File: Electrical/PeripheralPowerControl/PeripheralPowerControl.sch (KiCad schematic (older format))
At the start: 6 parts, among them J1 Conn_01x03, J2 Screw_Terminal_01x02, J3 Conn_01x03

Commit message: Adds ground plane to the peripheral board
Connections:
- net GND: now reaches BUCK1.1 (IN-), J1.1 (Pin_1), J3.1 (Pin_1)
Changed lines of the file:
@@
 	2850 1150 2850 1900
 Connection ~ 2850 1900
+$Comp
+L power:GND #PWR?
+U 1 1 5D95AD47
+P 2850 3900
+F 0 "#PWR?" H 2850 3650 50  0001 C CNN
+F 1 "GND" H 2855 3727 50  0000 C CNN
+F 2 "" H 2850 3900 50  0001 C CNN
+F 3 "" H 2850 3900 50  0001 C CNN
+	1    2850 3900
+	1    0    0    -1
+$EndComp
+Connection ~ 2850 3900
 $EndSCHEMATC

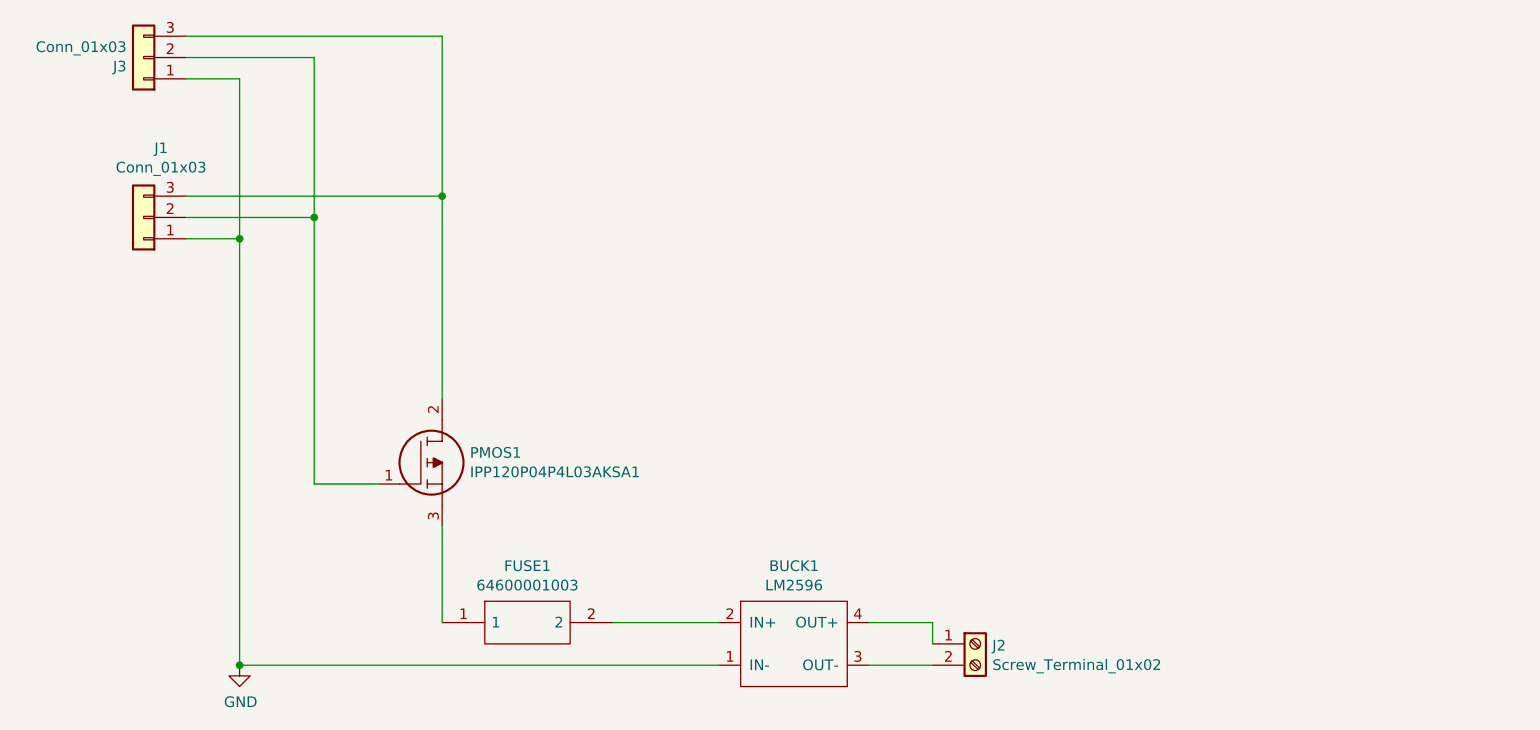
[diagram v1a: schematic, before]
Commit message: Verified Peripheral and Motor power controllers
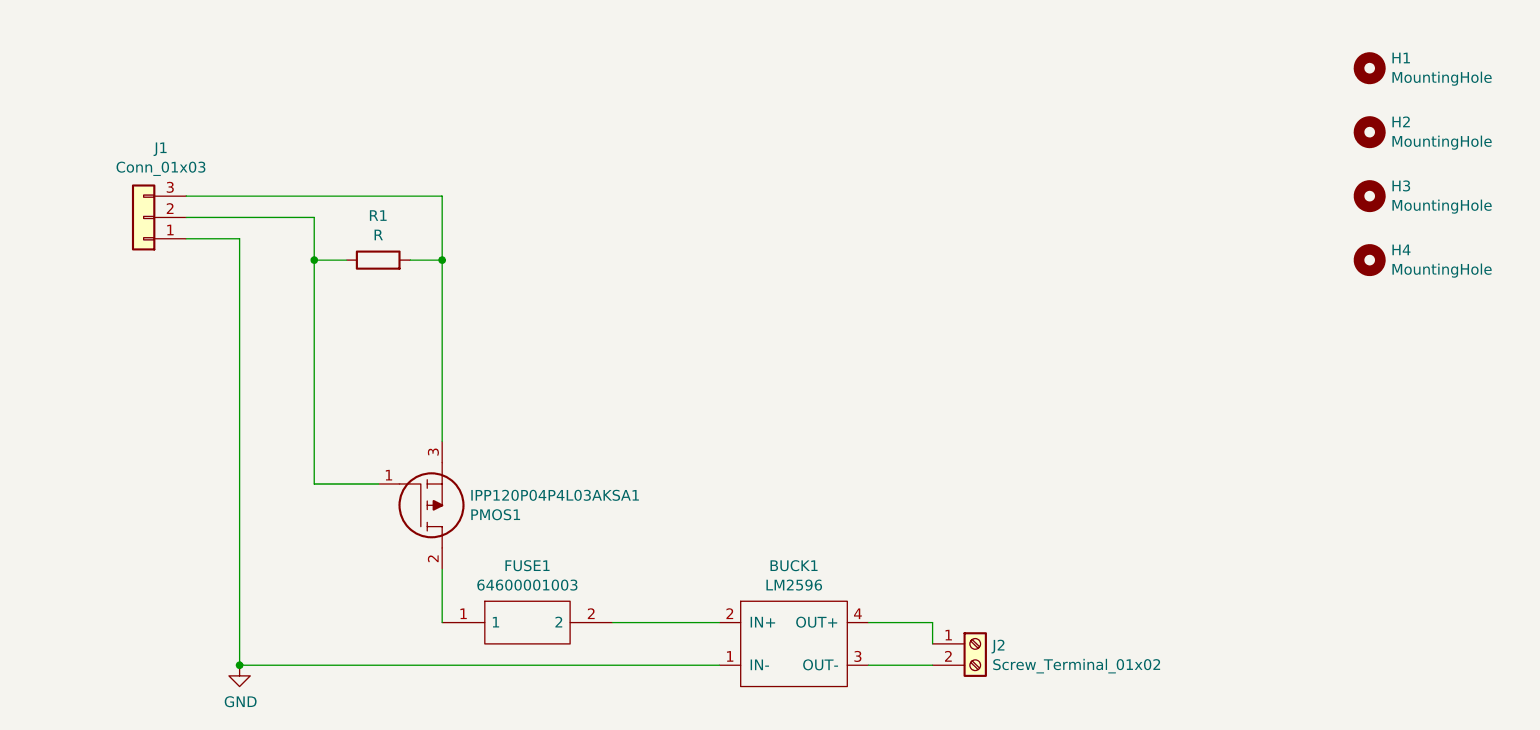
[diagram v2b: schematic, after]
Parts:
- removed J3: Conn_01x03, Connector_PinSocket_2.54mm:PinSocket_1x03_P2.54mm_Horizontal, symbol Connector_Generic:Conn_01x03
- added H1, H2, H3, H4: MountingHole, MountingHole:MountingHole_3.2mm_M3, symbol Mechanical:MountingHole
- added R1: R, Resistor_THT:R_Axial_DIN0204_L3.6mm_D1.6mm_P7.62mm_Horizontal, symbol Device:R
- J1: footprint Connector_PinHeader_2.54mm:PinHeader_1x03_P2.54mm_Horizontal -> Connector_JST:JST_EH_B3B-EH-A_1x03_P2.50mm_Vertical
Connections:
- net at FUSE1.1: now also PMOS1.2; no longer PMOS1.3
- net at J1.2 (Pin_2), PMOS1.1: now also R1.1
- net at J1.3 (Pin_3): now also PMOS1.3, R1.2; no longer PMOS1.2
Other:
- moved on the sheet: PMOS1
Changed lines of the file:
@@
 F 9 "IPP120P04P4L03AKSA1" H 3950 2300 50  0001 L CNN "Manufacturer_Part_Number"
 	1    3500 3050
-	1    0    0    -1
+	1    0    0    1
 $EndComp
 Wire Wire Line
@@
 Wire Wire Line
 	5100 3700 4600 3700
-Wire Wire Line
-	3800 3250 3800 3700
 $Comp
 L Connector_Generic:Conn_01x03 J1
@@
 F 0 "J1" H 2318 1475 50  0000 C CNN
 F 1 "Conn_01x03" H 2318 1566 50  0000 C CNN
-F 2 "Connector_PinHeader_2.54mm:PinHeader_1x03_P2.54mm_Horizontal" H 2400 1800 50  0001 C CNN
+F 2 "Connector_JST:JST_EH_B3B-EH-A_1x03_P2.50mm_Vertical" H 2400 1800 50  0001 C CNN
 F 3 "~" H 2400 1800 50  0001 C CNN
 	1    2400 1800
@@
 	2600 1700 3800 1700
 Wire Wire Line
-	3800 1700 3800 2650
-Wire Wire Line
 	2850 1900 2850 3900
 Wire Wire Line
-	3200 3050 3200 1800
+	3200 3050 3200 2000
 Wire Wire Line
 	3200 1800 2600 1800
-$Comp
-L Connector_Generic:Conn_01x03 J3
-U 1 1 5D94F2BA
-P 2400 1050
-F 0 "J3" H 2480 1092 50  0000 L CNN
-F 1 "Conn_01x03" H 2480 1001 50  0000 L CNN
-F 2 "Connector_PinSocket_2.54mm:PinSocket_1x03_P2.54mm_Horizontal" H 2400 1050 50  0001 C CNN
-F 3 "~" H 2400 1050 50  0001 C CNN
-	1    2400 1050
-	-1   0    0    1
-$EndComp
-Wire Wire Line
-	2600 950  3800 950
-Wire Wire Line
-	3800 950  3800 1700
-Connection ~ 3800 1700
-Wire Wire Line
-	3200 1800 3200 1050
-Wire Wire Line
-	3200 1050 2600 1050
-Connection ~ 3200 1800
 Wire Wire Line
 	2850 3900 5100 3900
 Wire Wire Line
 	2850 1900 2600 1900
-Wire Wire Line
-	2600 1150 2850 1150
-Wire Wire Line
-	2850 1150 2850 1900
-Connection ~ 2850 1900
 $Comp
-L power:GND #PWR?
+L power:GND #PWR0101
 U 1 1 5D95AD47
 P 2850 3900
-F 0 "#PWR?" H 2850 3650 50  0001 C CNN
+F 0 "#PWR0101" H 2850 3650 50  0001 C CNN
 F 1 "GND" H 2855 3727 50  0000 C CNN
 F 2 "" H 2850 3900 50  0001 C CNN
@@
 $EndComp
 Connection ~ 2850 3900
+$Comp
+L Device:R R1
+U 1 1 5D9D0066
+P 3500 2000
+F 0 "R1" V 3707 2000 50  0000 C CNN
+F 1 "R" V 3616 2000 50  0000 C CNN
+F 2 "Resistor_THT:R_Axial_DIN0204_L3.6mm_D1.6mm_P7.62mm_Horizontal" V 3430 2000 50  0001 C CNN
+F 3 "~" H 3500 2000 50  0001 C CNN
+	1    3500 2000
+	0    -1   -1   0
+$EndComp
+Wire Wire Line
+	3800 1700 3800 2000
+Wire Wire Line
+	3650 2000 3800 2000
+Wire Wire Line
+	3350 2000 3200 2000
+Connection ~ 3200 2000
+Wire Wire Line
+	3200 2000 3200 1800
+$Comp
+L Mechanical:MountingHole H1
+U 1 1 5D9D353F
+P 8150 1100
+F 0 "H1" H 8250 1146 50  0000 L CNN
+F 1 "MountingHole" H 8250 1055 50  0000 L CNN
+F 2 "MountingHole:MountingHole_3.2mm_M3" H 8150 1100 50  0001 C CNN
+F 3 "~" H 8150 1100 50  0001 C CNN
+	1    8150 1100
+	1    0    0    -1
+$EndComp
+$Comp
+L Mechanical:MountingHole H2
+U 1 1 5D9D3D3A
+P 8150 1400
+F 0 "H2" H 8250 1446 50  0000 L CNN
+F 1 "MountingHole" H 8250 1355 50  0000 L CNN
+F 2 "MountingHole:MountingHole_3.2mm_M3" H 8150 1400 50  0001 C CNN
+F 3 "~" H 8150 1400 50  0001 C CNN
+	1    8150 1400
+	1    0    0    -1
+$EndComp
+$Comp
+L Mechanical:MountingHole H3
+U 1 1 5D9D44B2
+P 8150 1700
+F 0 "H3" H 8250 1746 50  0000 L CNN
+F 1 "MountingHole" H 8250 1655 50  0000 L CNN
+F 2 "MountingHole:MountingHole_3.2mm_M3" H 8150 1700 50  0001 C CNN
+F 3 "~" H 8150 1700 50  0001 C CNN
+	1    8150 1700
+	1    0    0    -1
+$EndComp
+$Comp
+L Mechanical:MountingHole H4
+U 1 1 5D9D4DB1
+P 8150 2000
+F 0 "H4" H 8250 2046 50  0000 L CNN
+F 1 "MountingHole" H 8250 1955 50  0000 L CNN
+F 2 "MountingHole:MountingHole_3.2mm_M3" H 8150 2000 50  0001 C CNN
+F 3 "~" H 8150 2000 50  0001 C CNN
+	1    8150 2000
+	1    0    0    -1
+$EndComp
+Wire Wire Line
+	3800 2850 3800 2000
+Connection ~ 3800 2000
+Wire Wire Line
+	3800 3450 3800 3700
 $EndSCHEMATC

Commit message: Adds notes for the peripheral power controller
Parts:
- FUSE1: symbol LibraryLoader:64600001003 -> PeripheralPowerControl-rescue:64600001003-LibraryLoader
- PMOS1: symbol LibraryLoader:IPP120P04P4L03AKSA1 -> PeripheralPowerControl-rescue:IPP120P04P4L03AKSA1-LibraryLoader
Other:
- note added: "100K pull-up resistor\n"
- note added: "1: Peripheral Vcc\n2: Peripheral GND"
- note added: "3: Vcc\n2: Enable\n1: Ground"
- note added: "PMOS used to enable and disable\nthe peripheral"
- note added: "The pull-up resistor is used to\nensure power is cut to the\nperipheral when the enable signal\nis disconnected\n"
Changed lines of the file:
@@
 EESchema Schematic File Version 4
-LIBS:PeripheralPowerControl-cache
 EELAYER 30 0
 EELAYER END
@@
 $EndDescr
 $Comp
-L LibraryLoader:64600001003 FUSE1
+L PeripheralPowerControl-rescue:64600001003-LibraryLoader FUSE1
 U 1 1 5D945058
 P 3800 3700
@@
 $EndComp
 $Comp
-L LibraryLoader:IPP120P04P4L03AKSA1 PMOS1
+L PeripheralPowerControl-rescue:IPP120P04P4L03AKSA1-LibraryLoader PMOS1
 U 1 1 5D945064
 P 3500 3050
@@
 Wire Wire Line
 	5100 3700 4600 3700
+Wire Wire Line
+	2850 1900 2850 3900
+Wire Wire Line
+	3200 3050 3200 2000
+Wire Wire Line
+	2850 3900 5100 3900
+$Comp
+L power:GND #PWR0101
+U 1 1 5D95AD47
+P 2850 3900
+F 0 "#PWR0101" H 2850 3650 50  0001 C CNN
+F 1 "GND" H 2855 3727 50  0000 C CNN
+F 2 "" H 2850 3900 50  0001 C CNN
+F 3 "" H 2850 3900 50  0001 C CNN
+	1    2850 3900
+	1    0    0    -1
+$EndComp
+Connection ~ 2850 3900
+$Comp
+L Device:R R1
+U 1 1 5D9D0066
+P 3500 2000
+F 0 "R1" V 3707 2000 50  0000 C CNN
+F 1 "R" V 3616 2000 50  0000 C CNN
+F 2 "Resistor_THT:R_Axial_DIN0204_L3.6mm_D1.6mm_P7.62mm_Horizontal" V 3430 2000 50  0001 C CNN
+F 3 "~" H 3500 2000 50  0001 C CNN
+	1    3500 2000
+	0    -1   -1   0
+$EndComp
+Wire Wire Line
+	3800 1700 3800 2000
+Wire Wire Line
+	3650 2000 3800 2000
+Wire Wire Line
+	3350 2000 3200 2000
+Connection ~ 3200 2000
+Wire Wire Line
+	3200 2000 3200 1800
+$Comp
+L Mechanical:MountingHole H1
+U 1 1 5D9D353F
+P 8150 1100
+F 0 "H1" H 8250 1146 50  0000 L CNN
+F 1 "MountingHole" H 8250 1055 50  0000 L CNN
+F 2 "MountingHole:MountingHole_3.2mm_M3" H 8150 1100 50  0001 C CNN
+F 3 "~" H 8150 1100 50  0001 C CNN
+	1    8150 1100
+	1    0    0    -1
+$EndComp
+$Comp
+L Mechanical:MountingHole H2
+U 1 1 5D9D3D3A
+P 8150 1400
+F 0 "H2" H 8250 1446 50  0000 L CNN
+F 1 "MountingHole" H 8250 1355 50  0000 L CNN
+F 2 "MountingHole:MountingHole_3.2mm_M3" H 8150 1400 50  0001 C CNN
+F 3 "~" H 8150 1400 50  0001 C CNN
+	1    8150 1400
+	1    0    0    -1
+$EndComp
+$Comp
+L Mechanical:MountingHole H3
+U 1 1 5D9D44B2
+P 8150 1700
+F 0 "H3" H 8250 1746 50  0000 L CNN
+F 1 "MountingHole" H 8250 1655 50  0000 L CNN
+F 2 "MountingHole:MountingHole_3.2mm_M3" H 8150 1700 50  0001 C CNN
+F 3 "~" H 8150 1700 50  0001 C CNN
+	1    8150 1700
+	1    0    0    -1
+$EndComp
+$Comp
+L Mechanical:MountingHole H4
+U 1 1 5D9D4DB1
+P 8150 2000
+F 0 "H4" H 8250 2046 50  0000 L CNN
+F 1 "MountingHole" H 8250 1955 50  0000 L CNN
+F 2 "MountingHole:MountingHole_3.2mm_M3" H 8150 2000 50  0001 C CNN
+F 3 "~" H 8150 2000 50  0001 C CNN
+	1    8150 2000
+	1    0    0    -1
+$EndComp
+Wire Wire Line
+	3800 2850 3800 2000
+Connection ~ 3800 2000
+Wire Wire Line
+	3800 3450 3800 3700
+Wire Wire Line
+	2850 1900 2600 1900
+Wire Wire Line
+	3200 1800 2600 1800
+Wire Wire Line
+	2600 1700 3800 1700
 $Comp
 L Connector_Generic:Conn_01x03 J1
@@
 	-1   0    0    1
 $EndComp
-Wire Wire Line
-	2600 1700 3800 1700
-Wire Wire Line
-	2850 1900 2850 3900
-Wire Wire Line
-	3200 3050 3200 2000
-Wire Wire Line
-	3200 1800 2600 1800
-Wire Wire Line
-	2850 3900 5100 3900
-Wire Wire Line
-	2850 1900 2600 1900
-$Comp
-L power:GND #PWR0101
-U 1 1 5D95AD47
-P 2850 3900
-F 0 "#PWR0101" H 2850 3650 50  0001 C CNN
-F 1 "GND" H 2855 3727 50  0000 C CNN
-F 2 "" H 2850 3900 50  0001 C CNN
-F 3 "" H 2850 3900 50  0001 C CNN
-	1    2850 3900
-	1    0    0    -1
-$EndComp
-Connection ~ 2850 3900
-$Comp
-L Device:R R1
-U 1 1 5D9D0066
-P 3500 2000
-F 0 "R1" V 3707 2000 50  0000 C CNN
-F 1 "R" V 3616 2000 50  0000 C CNN
-F 2 "Resistor_THT:R_Axial_DIN0204_L3.6mm_D1.6mm_P7.62mm_Horizontal" V 3430 2000 50  0001 C CNN
-F 3 "~" H 3500 2000 50  0001 C CNN
-	1    3500 2000
-	0    -1   -1   0
-$EndComp
-Wire Wire Line
-	3800 1700 3800 2000
-Wire Wire Line
-	3650 2000 3800 2000
-Wire Wire Line
-	3350 2000 3200 2000
-Connection ~ 3200 2000
-Wire Wire Line
-	3200 2000 3200 1800
-$Comp
-L Mechanical:MountingHole H1
-U 1 1 5D9D353F
-P 8150 1100
-F 0 "H1" H 8250 1146 50  0000 L CNN
-F 1 "MountingHole" H 8250 1055 50  0000 L CNN
-F 2 "MountingHole:MountingHole_3.2mm_M3" H 8150 1100 50  0001 C CNN
-F 3 "~" H 8150 1100 50  0001 C CNN
-	1    8150 1100
-	1    0    0    -1
-$EndComp
-$Comp
-L Mechanical:MountingHole H2
-U 1 1 5D9D3D3A
-P 8150 1400
-F 0 "H2" H 8250 1446 50  0000 L CNN
-F 1 "MountingHole" H 8250 1355 50  0000 L CNN
-F 2 "MountingHole:MountingHole_3.2mm_M3" H 8150 1400 50  0001 C CNN
-F 3 "~" H 8150 1400 50  0001 C CNN
-	1    8150 1400
-	1    0    0    -1
-$EndComp
-$Comp
-L Mechanical:MountingHole H3
-U 1 1 5D9D44B2
-P 8150 1700
-F 0 "H3" H 8250 1746 50  0000 L CNN
-F 1 "MountingHole" H 8250 1655 50  0000 L CNN
-F 2 "MountingHole:MountingHole_3.2mm_M3" H 8150 1700 50  0001 C CNN
-F 3 "~" H 8150 1700 50  0001 C CNN
-	1    8150 1700
-	1    0    0    -1
-$EndComp
-$Comp
-L Mechanical:MountingHole H4
-U 1 1 5D9D4DB1
-P 8150 2000
-F 0 "H4" H 8250 2046 50  0000 L CNN
-F 1 "MountingHole" H 8250 1955 50  0000 L CNN
-F 2 "MountingHole:MountingHole_3.2mm_M3" H 8150 2000 50  0001 C CNN
-F 3 "~" H 8150 2000 50  0001 C CNN
-	1    8150 2000
-	1    0    0    -1
-$EndComp
-Wire Wire Line
-	3800 2850 3800 2000
-Connection ~ 3800 2000
-Wire Wire Line
-	3800 3450 3800 3700
+Text Notes 1960 1920 0    50   ~ 0
+3: Vcc\n2: Enable\n1: Ground
+Text Notes 3130 1630 0    50   ~ 0
+100K pull-up resistor\n
+Text Notes 3920 2220 0    50   ~ 0
+The pull-up resistor is used to\nensure power is cut to the\nperipheral when the enable signal\nis disconnected\n
+Text Notes 3950 2960 0    50   ~ 0
+PMOS used to enable and disable\nthe peripheral
+Text Notes 6540 3810 0    50   ~ 0
+1: Peripheral Vcc\n2: Peripheral GND
 $EndSCHEMATC
